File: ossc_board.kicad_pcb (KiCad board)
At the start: 2 copper layers, 124.6 x 68.7 mm, 238 parts, among them J1 VGA, J10 CLK9, J11 CLK8, J12 CLK2, J13 SD_CLK, J2 3XRCA_CONN, J21 I2C_BCK, J22 I2C_WS, J23 I2C_DATA, J24 I2C_MCLK, J3 SCART-F, J4 HDMI_CONN, J5 5VDC_IN, J6 SJ1-3533NG, J7 SJ1-3533NG, P1 JTAG_CONN, P3 mSD_CONN, Q1 BC847, Q2 BC857, SW1 SPST, SW2 SW_PUSH, SW3 SW_PUSH, SW4 DPDT, U1 TVP7002PZP, U10 S25FL216K, U11 IRM-V538/TR1, U12 TLV70012, U13 TLV70025, U14 TLV70012, U15 TLV70018, U16 TLV70018, U17 THS7353, U2 EP4CE15E22, U3 IT6613, U4 SN74LVC2G17, U5 AP7361C, U6 TLV70033, U7 NCP703SN19T1G, U8 PCM1862, U9 TLV70019, Y1 ACHL-27MHZ-EK, Y2 24.576MHz

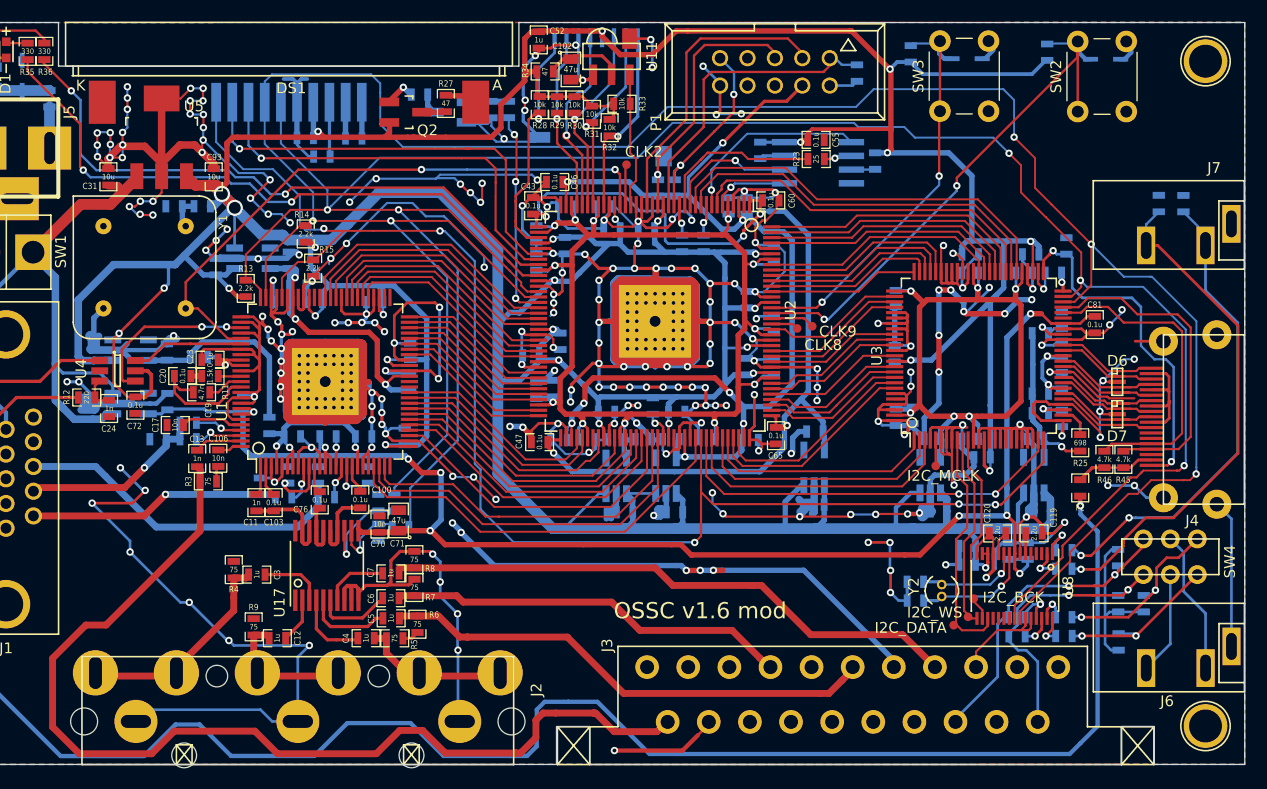
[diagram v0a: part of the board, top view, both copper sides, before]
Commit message: remove unnecessary component
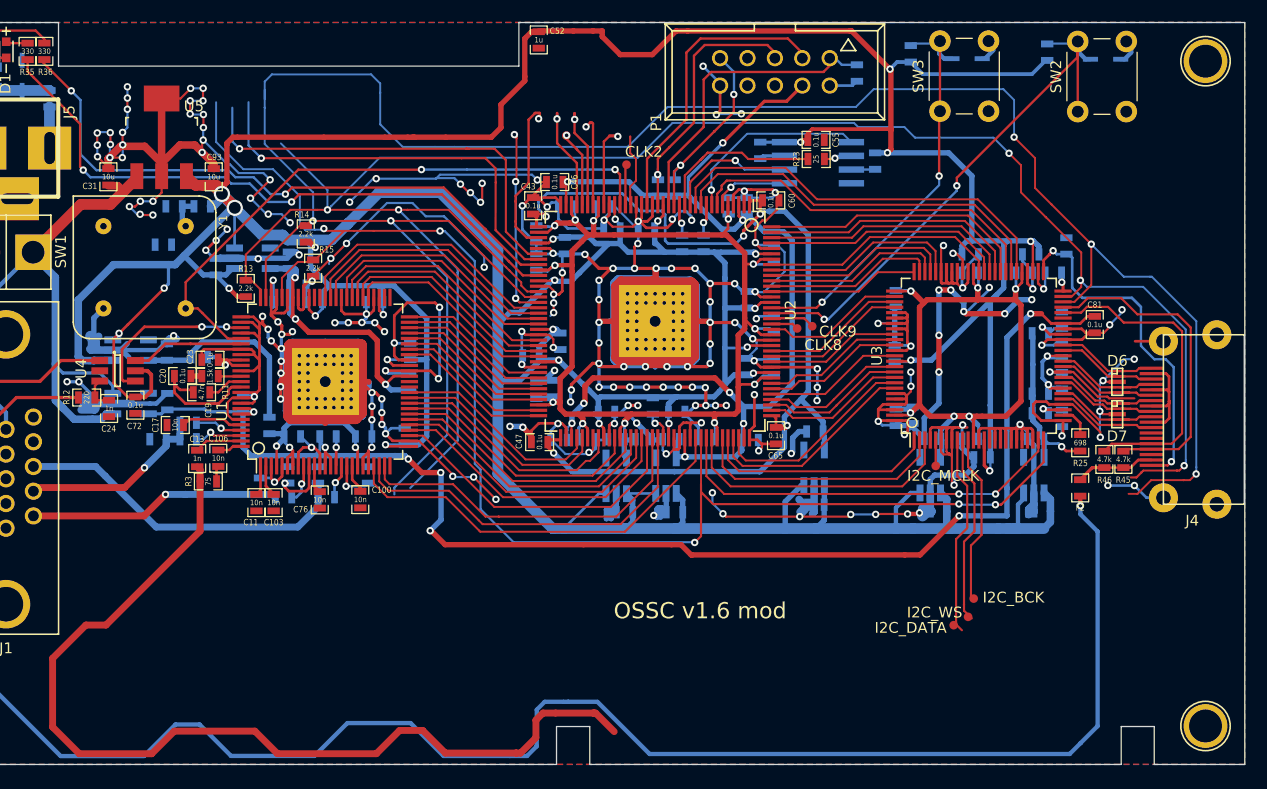
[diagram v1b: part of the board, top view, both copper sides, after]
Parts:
- removed C102, C71: 47u, custom_components:SM0805_libcms
- removed C111, C112: 30p, custom_components:SM0603_Capa_libcms
- removed C113, C115, C116, C121, C123, C124, C125, C126: 10u, custom_components:SM0603_Capa_libcms
- removed C114, C118: 0.1u, custom_components:SM0603_Capa_libcms
- removed C119, C120: 2.2u, custom_components:SM0603_Capa_libcms
- removed C12, C29, C3, C30, C4, C5, C56, C6, C7: 1u, custom_components:SM0603_Capa_libcms
- removed C36: 22p, custom_components:SM0603_Capa_libcms
- removed C70: 10n, custom_components:SM0603_Capa_libcms
- removed DS1: CONN_01X12, custom_components:NHD-C0216CZ_vertmount
- removed J2: 3XRCA_CONN, custom_components:3xRCA_CONN
- removed J3: SCART-F, custom_components:SCART_CONN
- removed J6, J7: SJ1-3533NG, custom_components:SJ1-3533NG
- removed P3: mSD_CONN, custom_components:DM3D-SF
- removed Q1: BC847, Housings_SOT-23_SOT-143_TSOT-6:SOT-23_Handsoldering
- removed Q2: BC857, Housings_SOT-23_SOT-143_TSOT-6:SOT-23_Handsoldering
- removed R27, R34: 47, custom_components:SM0603_Resistor_libcms
- removed R28, R29, R30, R31, R32, R33, R39: 10k, custom_components:SM0603_Resistor_libcms
- removed R37, R40: 1k, custom_components:SM0603_Resistor_libcms
- removed R38, R44: 100, custom_components:SM0603_Resistor_libcms
- removed R4, R5, R6, R7, R8, R9: 75, custom_components:SM0603_Resistor_libcms
- removed R47, R48, R49, R50, R51, R52: 100k, custom_components:SM0603_Resistor_libcms
- removed SW4: DPDT, custom_components:MS22
- removed U11: IRM-V538/TR1, custom_components:IRM-V5XX_TR1
- removed U17: THS7353, custom_components:TSSOP-20_4.4x6.5mm_Pitch0.65mm_Handsoldering
- removed U8: PCM1862, custom_components:TSSOP-30_4.4x7.8mm_Pitch0.5mm_Handsoldering
- removed Y2: 24.576MHz, custom_components:ECS-3X9X
- C100, C103, C76: value 0.1u -> 10n
- C11: value 1n -> 10n
- C33: value 22p -> 1u
- moved C33 31.1 mm to (31.7, 37.6), turned to 180 degrees
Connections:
- net /fpga1/SD_CLK renamed Net-(J13-Pad1)
- C100 pad 1: /tvp_board1/RGB_12_B -> GND
- C103 pad 1: /tvp_board1/RGB_12_G -> GND
- C11 pad 1: /tvp_board1/RGB_12_G -> GND
- C33 pad 1: GND -> Net-(C25-Pad1)
- C33 pad 2: Net-(C33-Pad2) -> GND
- C76 pad 1: /tvp_board1/RGB_12_R -> GND
- U2 pad 23: /fpga1/IR_RX -> Net-(U2-Pad23)
- U2 pad 28: /fpga1/SD_DAT2 -> Net-(U2-Pad28)
- U2 pad 30: /fpga1/SD_DAT3 -> Net-(U2-Pad30)
- U2 pad 31: /fpga1/SD_CMD -> Net-(U2-Pad31)
- U2 pad 33: /fpga1/SD_DAT0 -> Net-(U2-Pad33)
- U2 pad 39: /fpga1/SD_DAT1 -> Net-(U2-Pad39)
- U2 pad 42: /fpga1/LCD_RS -> Net-(U2-Pad42)
- U2 pad 43: /fpga1/LCD_CS_N -> Net-(U2-Pad43)
- U2 pad 51: /fpga1/LCD_BLEN -> Net-(U2-Pad51)
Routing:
- net GND: track 1356.9 -> 1076.0 mm, vias 239 -> 206
- net /tvp_board1/RGB1_B: track 53.8 -> 0.00 mm
- net /hdmitx1/AV3_AUD_R: track 47.3 -> 0.00 mm, vias 1 -> 0
- net /tvp_board1/RGB1_G: track 46.3 -> 0.00 mm
- net /hdmitx1/AV3_AUD_L: track 44.1 -> 0.00 mm, vias 2 -> 0
- net Net-(U2-Pad42): track 0.00 -> 40.0 mm, vias 0 -> 1
- net /fpga1/LCD_RS: track 40.0 -> 0.00 mm, vias 1 -> 0
- net Net-(U2-Pad43): track 0.00 -> 38.6 mm, vias 0 -> 1
- net /fpga1/LCD_CS_N: track 38.6 -> 0.00 mm, vias 1 -> 0
- net /tvp_board1/RGB1_R: track 37.2 -> 0.00 mm
- net /hdmitx1/AV1_AUD_L: track 29.4 -> 0.00 mm, vias 2 -> 0
- net /hdmitx1/AV1_AUD_R: track 27.0 -> 0.00 mm, vias 2 -> 0
- net /hdmitx1/DVDD3V3: track 614.8 -> 588.9 mm, vias 32 -> 29
- net /fpga1/SDA: track 214.1 -> 189.6 mm
- net /fpga1/SD_DAT1: track 23.5 -> 0.00 mm, vias 1 -> 0
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
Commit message: update the tracks
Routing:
- net /tvp_board1/RGB1_S: track 90.9 -> 1.47 mm
- net GND: track 1076.0 -> 1059.0 mm
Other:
- board text removed: "OSSC v1.6 mod"
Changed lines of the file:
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@@
   (general
     (thickness 1.6)
-    (drawings 17)
-    (tracks 3544)
+    (drawings 16)
+    (tracks 3514)
     (zones 0)
     (modules 173)
@@
     (user_trace_width 1)
     (trace_clearance 0.16)
-    (zone_clearance 0.16)
+    (zone_clearance 0.2)
     (zone_45_only yes)
     (trace_min 0.16)
@@
   )
   (gr_line (start 68.165 85.764) (end 7.368 85.764) (angle 90) (layer Edge.Cuts) (width 0.1))
-  (gr_text "OSSC v1.6 mod" (at 81.473 71.526) (layer F.SilkS)
-    (effects (font (size 1.5 1.5) (thickness 0.3)))
-  )
   (gr_line (start 68.165 82.25) (end 68.165 85.764) (angle 90) (layer Edge.Cuts) (width 0.1))
   (gr_line (start 71.244 82.25) (end 68.165 82.25) (angle 90) (layer Edge.Cuts) (width 0.1))
@@
   (segment (start 63.1512 47.9512) (end 56.3 41.1) (width 0.18) (layer F.Cu) (net 88))
   (segment (start 66.3145 47.9512) (end 63.1512 47.9512) (width 0.18) (layer F.Cu) (net 88))
-  (segment (start 71.613 80.9997) (end 71.7877 80.9997) (width 0.64) (layer F.Cu) (net 89))
-  (segment (start 71.7877 80.9997) (end 73.5116 82.7236) (width 0.64) (layer F.Cu) (net 89))
-  (segment (start 64.45 84.7081) (end 64.8349 84.7081) (width 0.64) (layer F.Cu) (net 89))
-  (segment (start 68.0804 80.9997) (end 71.613 80.9997) (width 0.64) (layer F.Cu) (net 89))
-  (segment (start 71.613 80.9997) (end 71.5541 80.9997) (width 0.64) (layer F.Cu) (net 89))
-  (segment (start 66.9123 80.9997) (end 68.0804 80.9997) (width 0.64) (layer F.Cu) (net 89))
-  (segment (start 66.256 81.656) (end 66.9123 80.9997) (width 0.64) (layer F.Cu) (net 89))
-  (segment (start 66.256 83.287) (end 66.256 81.656) (width 0.64) (layer F.Cu) (net 89))
-  (segment (start 64.8349 84.7081) (end 66.256 83.287) (width 0.64) (layer F.Cu) (net 89))
-  (segment (start 35.1387 59.5367) (end 35.1387 64.1341) (width 0.64) (layer F.Cu) (net 89))
-  (segment (start 57.859 84.7081) (end 64.45 84.7081) (width 0.64) (layer F.Cu) (net 89))
-  (segment (start 64.45 84.7081) (end 64.372 84.7081) (width 0.64) (layer F.Cu) (net 89))
-  (segment (start 55.7635 82.6126) (end 57.859 84.7081) (width 0.64) (layer F.Cu) (net 89))
-  (segment (start 53.6299 82.6126) (end 55.7635 82.6126) (width 0.64) (layer F.Cu) (net 89))
-  (segment (start 51.4737 84.7688) (end 53.6299 82.6126) (width 0.64) (layer F.Cu) (net 89))
-  (segment (start 42.3114 84.7688) (end 51.4737 84.7688) (width 0.64) (layer F.Cu) (net 89))
-  (segment (start 40.2187 82.6761) (end 42.3114 84.7688) (width 0.64) (layer F.Cu) (net 89))
-  (segment (start 32.7511 82.6761) (end 40.2187 82.6761) (width 0.64) (layer F.Cu) (net 89))
-  (segment (start 30.6556 84.7716) (end 32.7511 82.6761) (width 0.64) (layer F.Cu) (net 89))
-  (segment (start 23.95 84.7716) (end 30.6556 84.7716) (width 0.64) (layer F.Cu) (net 89))
-  (segment (start 21.4735 82.2951) (end 23.95 84.7716) (width 0.64) (layer F.Cu) (net 89))
-  (segment (start 21.4735 75.9324) (end 21.4735 82.2951) (width 0.64) (layer F.Cu) (net 89))
-  (segment (start 24.5596 72.8463) (end 21.4735 75.9324) (width 0.64) (layer F.Cu) (net 89))
-  (segment (start 26.4265 72.8463) (end 24.5596 72.8463) (width 0.64) (layer F.Cu) (net 89))
-  (segment (start 35.1387 64.1341) (end 26.4265 72.8463) (width 0.64) (layer F.Cu) (net 89))
   (segment (start 35.1387 59.5367) (end 35.1387 58.4445) (width 0.64) (layer F.Cu) (net 89))
   (segment (start 35.1387 58.4445) (end 34.872 58.1778) (width 0.64) (layer F.Cu) (net 89))
@@
   (segment (start 61.3156 63.5) (end 60.9588 63.1432) (width 0.18) (layer F.Cu) (net 93))
   (segment (start 15.549 20.2943) (end 14.6457 20.2943) (width 0.25) (layer F.Cu) (net 94))
-  (segment (start 14.23 20.71) (end 14.23 27.67634) (width 0.25) (layer F.Cu) (net 94))
   (segment (start 14.6457 20.2943) (end 14.23 20.71) (width 0.25) (layer F.Cu) (net 94))
-  (segment (start 14.23 27.67634) (end 15.20266 28.649) (width 0.25) (layer F.Cu) (net 94))
-  (segment (start 15.20266 28.649) (end 15.20266 30.34826) (width 0.25) (layer B.Cu) (net 94))
-  (segment (start 15.20266 30.34826) (end 18.2024 33.348) (width 0.25) (layer B.Cu) (net 94))
   (segment (start 103.8 40.1) (end 103.8 37.9) (width 0.2) (layer F.Cu) (net 94))
   (via (at 104.02 37.68) (size 0.686) (drill 0.35) (layers F.Cu B.Cu) (net 94))
@@
   (segment (start 77.4 44.6) (end 77.3 44.7) (width 0.5) (layer F.Cu) (net 94))
   (segment (start 77.4 39.8) (end 77.4 44.6) (width 0.5) (layer F.Cu) (net 94))
-  (segment (start 75.4 42.8) (end 77.3 44.7) (width 0.5) (layer F.Cu) (net 94))
   (segment (start 75.738 36.1) (end 75.738 37.462) (width 0.25) (layer B.Cu) (net 94))
   (segment (start 75.4 37.8) (end 75.4 39.8) (width 0.25) (layer F.Cu) (net 94))
@@
   (segment (start 69.8351 27.2533) (end 69.8351 25.4118) (width 0.22) (layer F.Cu) (net 175))
   (zone (net 94) (net_name GND) (layer F.Cu) (hatch edge 0.508)
-    (connect_pads (clearance 0.16))
+    (connect_pads (clearance 0.2))
     (min_thickness 0.2)
-    (fill yes (arc_segments 16) (thermal_gap 0.508) (thermal_bridge_width 0.508))
+    (fill yes (arc_segments 16) (thermal_gap 0.5) (thermal_bridge_width 0.5))
     (polygon
       (pts
@@
   )
   (zone (net 94) (net_name GND) (layer B.Cu) (hatch edge 0.508)
-    (connect_pads (clearance 0.16))
+    (connect_pads (clearance 0.2))
     (min_thickness 0.2)
-    (fill yes (arc_segments 16) (thermal_gap 0.508) (thermal_bridge_width 0.508))
+    (fill yes (arc_segments 16) (thermal_gap 0.5) (thermal_bridge_width 0.5))
     (polygon
       (pts
